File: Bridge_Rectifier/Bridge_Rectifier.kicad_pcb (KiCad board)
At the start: 2 copper layers, 87 x 30.5 mm, 7 parts, among them J1 Screw_Terminal_01x02, J2 Screw_Terminal_01x02

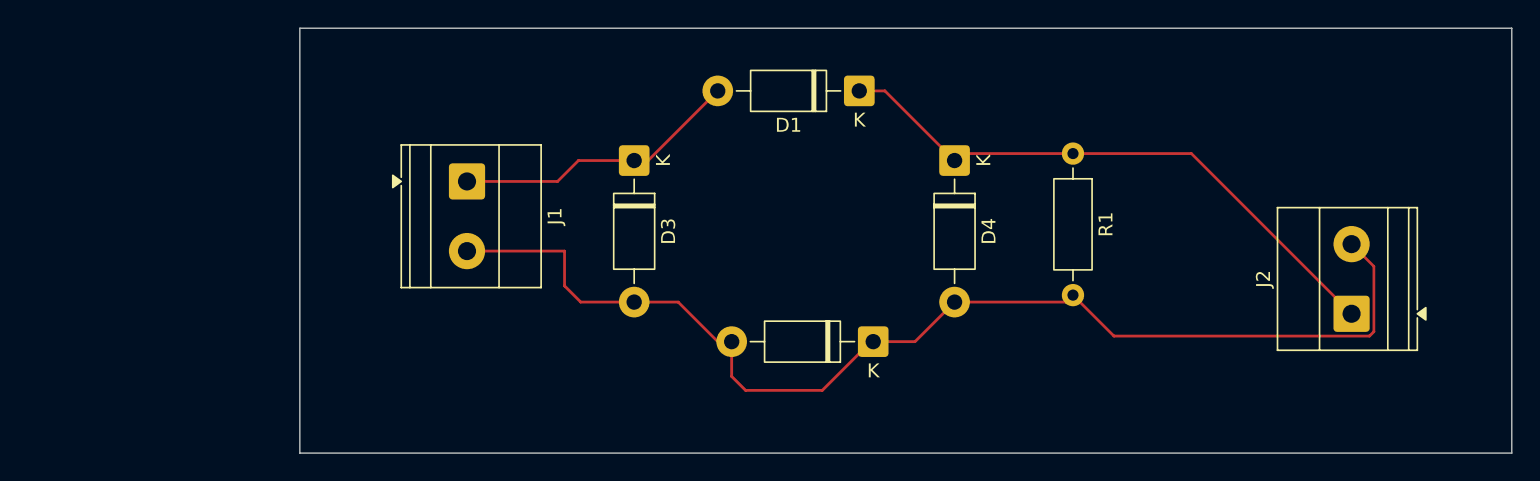
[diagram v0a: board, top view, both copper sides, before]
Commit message: Correct Footprint of transformer and reduced hole size
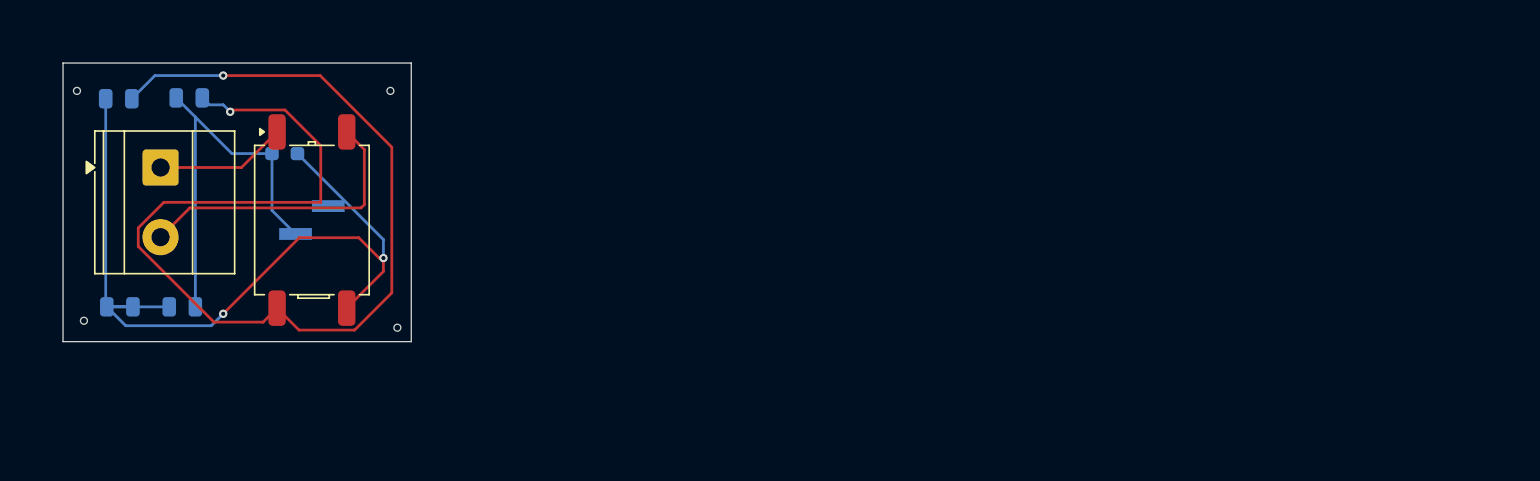
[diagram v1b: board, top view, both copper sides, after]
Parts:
- added H1: MountingHole, MountingHole:MountingHole_2.1mm, F.Cu at (92.0, 74.0)
- added H2: MountingHole, MountingHole:MountingHole_2.1mm, F.Cu at (92.5, 91.0)
- added H3: MountingHole, MountingHole:MountingHole_2.1mm, F.Cu at (69.5, 74.0)
- added H4: MountingHole, MountingHole:MountingHole_2.1mm, F.Cu at (70.0, 90.5)
- added T1: Transformer_1P_1S, Transformer_SMD:Transformer_ED8_4-Lead_10.5x8mm_P5mm, F.Cu at (86.4, 83.3)
- D1, D2, D3, D4: footprint Diode_THT:D_DO-41_SOD81_P10.16mm_Horizontal -> Diode_SMD:D_0805_2012Metric; moved to B.Cu
- J2: value Screw_Terminal_01x02 -> Conn_01x02_Pin; footprint TerminalBlock_Phoenix:TerminalBlock_Phoenix_MKDS-1,5-2_1x02_P5.00mm_Horizontal -> Connector_PinHeader_2.00mm:PinHeader_1x02_P2.00mm_Vertical_SMD_Pin1Left; moved to B.Cu
- R1: footprint Resistor_THT:R_Axial_DIN0207_L6.3mm_D2.5mm_P10.16mm_Horizontal -> Resistor_SMD:R_0603_1608Metric_Pad0.98x0.95mm_HandSolder; moved to B.Cu
- moved J2 74.9 mm to (86.4, 83.3), turned to 180 degrees
- moved R1 56.6 mm to (84.4, 78.5), turned to 0 degrees
- moved D4 56.4 mm to (77.1, 89.5), turned to 180 degrees
- moved D2 54.1 mm to (72.6, 89.5), turned to 0 degrees
- moved D1 48.1 mm to (77.6, 74.5), turned to 0 degrees
- moved D3 37.3 mm to (72.5, 74.6), turned to 180 degrees
- moved J1 22.0 mm to (75.5, 79.5)
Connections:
- J1 pad 1: Net-(D1-A) -> Net-(J1-Pin_1)
- J1 pad 2: Net-(D2-A) -> Net-(J1-Pin_2)
- J2 pad 1: Net-(D1-K) -> Net-(D2-A)
- J2 pad 2: Net-(D2-A) -> Net-(D1-K)
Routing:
- net Net-(D1-A): track 20.7 -> 83.8 mm, vias 0 -> 2
- net Net-(D2-A): track 84.3 -> 59.7 mm, vias 0 -> 2
- net Net-(J1-Pin_2): track 0.00 -> 21.3 mm
- net Net-(D1-K): track 42.4 -> 28.6 mm
- net Net-(J1-Pin_1): track 0.00 -> 9.42 mm
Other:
- board size 87 x 30.5 mm -> 25 x 20 mm

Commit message: Gerber files added
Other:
- board size 25 x 20 mm -> 29 x 22.5 mm
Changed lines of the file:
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@@
 		(filling no)
 		(pcbplotparams
-			(layerselection 0x00000000_00000000_55555555_5755f5ff)
+			(layerselection 0x00000000_00000000_55557fdf_57ffffff)
 			(plot_on_all_layers_selection 0x00000000_00000000_00000000_00000000)
 			(disableapertmacros no)
@@
 			(outputformat 1)
 			(mirror no)
-			(drillshape 1)
+			(drillshape 0)
 			(scaleselection 1)
 			(outputdirectory "")
@@
 	)
 	(gr_rect
-		(start 68.5 72)
-		(end 93.5 92)
+		(start 66 71)
+		(end 95 93.5)
 		(stroke
 			(width 0.05)
